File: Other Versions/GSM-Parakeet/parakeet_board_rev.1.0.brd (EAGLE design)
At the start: 33.5 x 38.5 mm, 15 parts

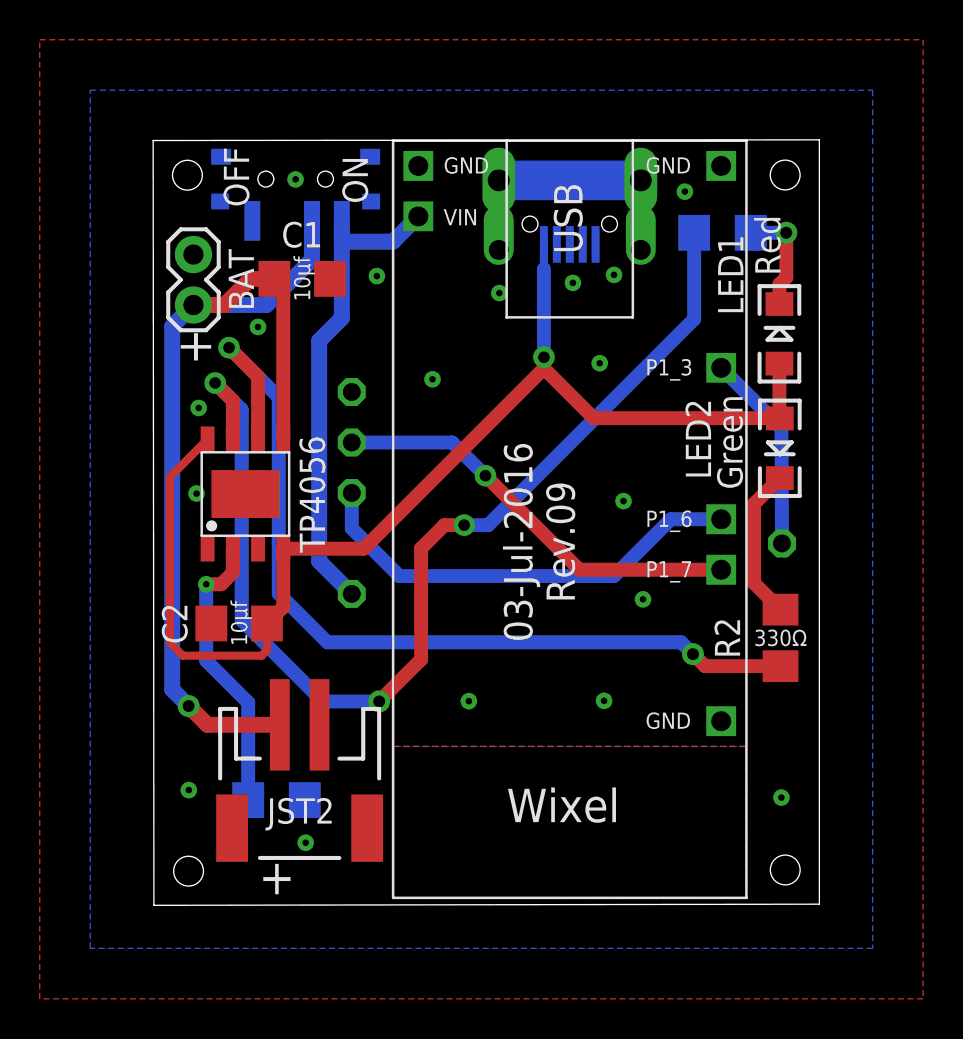
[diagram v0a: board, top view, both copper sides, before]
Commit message: updated parakeet version
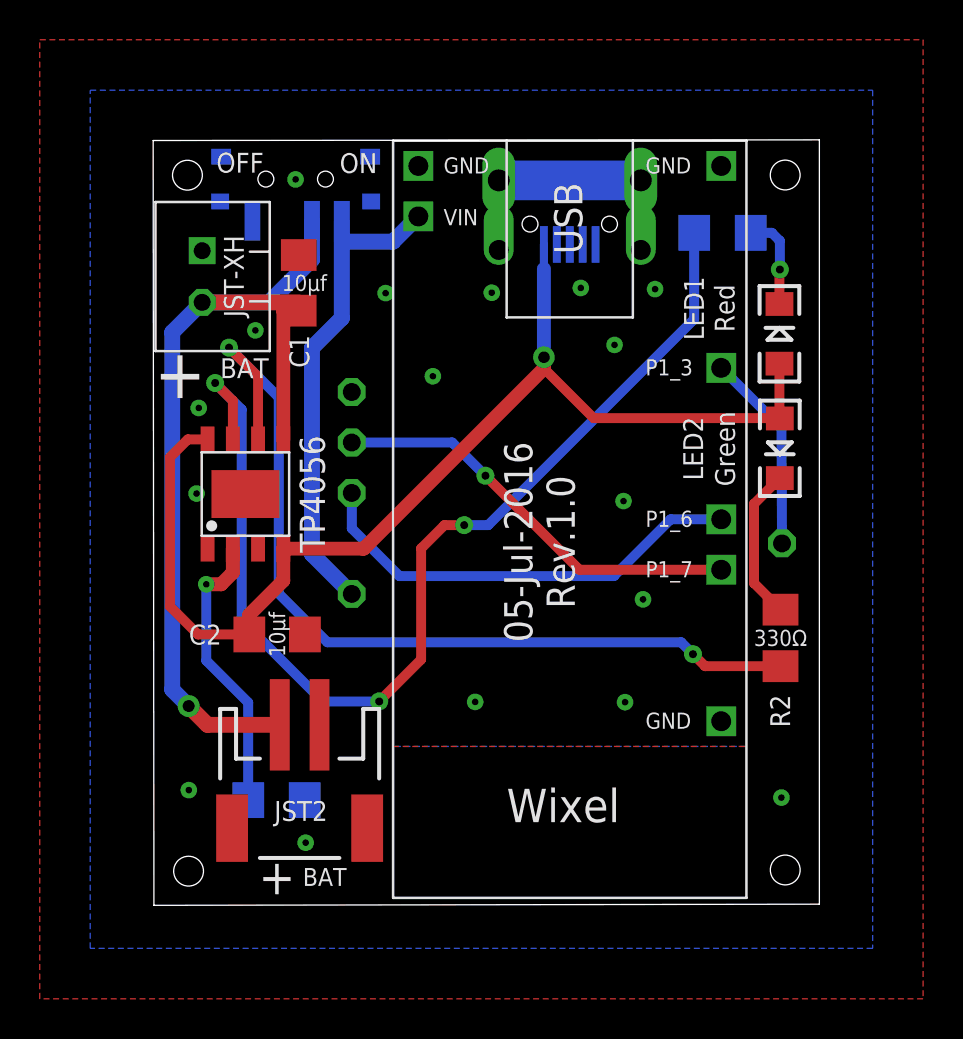
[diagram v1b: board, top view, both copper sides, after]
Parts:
- removed +: BAT, SparkFun-Connectors:1X02
- added JST-XH: 2_PIN_JST-XH-B2B, JST-XH_HEADERS:2_PIN_JST-XH-B2B
- moved C2 1.99 mm to (8.13, 55.2), turned to 0 degrees
- moved C1 0.26 mm to (9.22, 72.9), turned to 90 degrees
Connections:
- net GND: now also JST-XH.P$2; no longer +.2
- net N$8: now also JST-XH.P$1; no longer +.1
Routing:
- net N$7: track 60.6 -> 58.2 mm
- net N$8: track 47.9 -> 47.2 mm
- net N$3: track 5.52 -> 4.82 mm
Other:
- board text added: "+"
- board text added: "05-Jul-2016 Rev.1.0"
- board text added: "BAT"
- board text added: "JST-XH"
- board text removed: "03-Jul-2016 Rev.09"
